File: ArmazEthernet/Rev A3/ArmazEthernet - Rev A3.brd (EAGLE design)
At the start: 72 x 80 mm, 125 parts, among them J1 22-05-7028-02, P1 RB1-125BAG1A, T1 H1102FNL, T2 H1102FNL, U1 TC1264-3.3, U2 TC1264-1.8, U3 KSZ8995MA, U4 AT24C02C-SSHM-B, X1 NE8FAV, X2 NE8FAV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

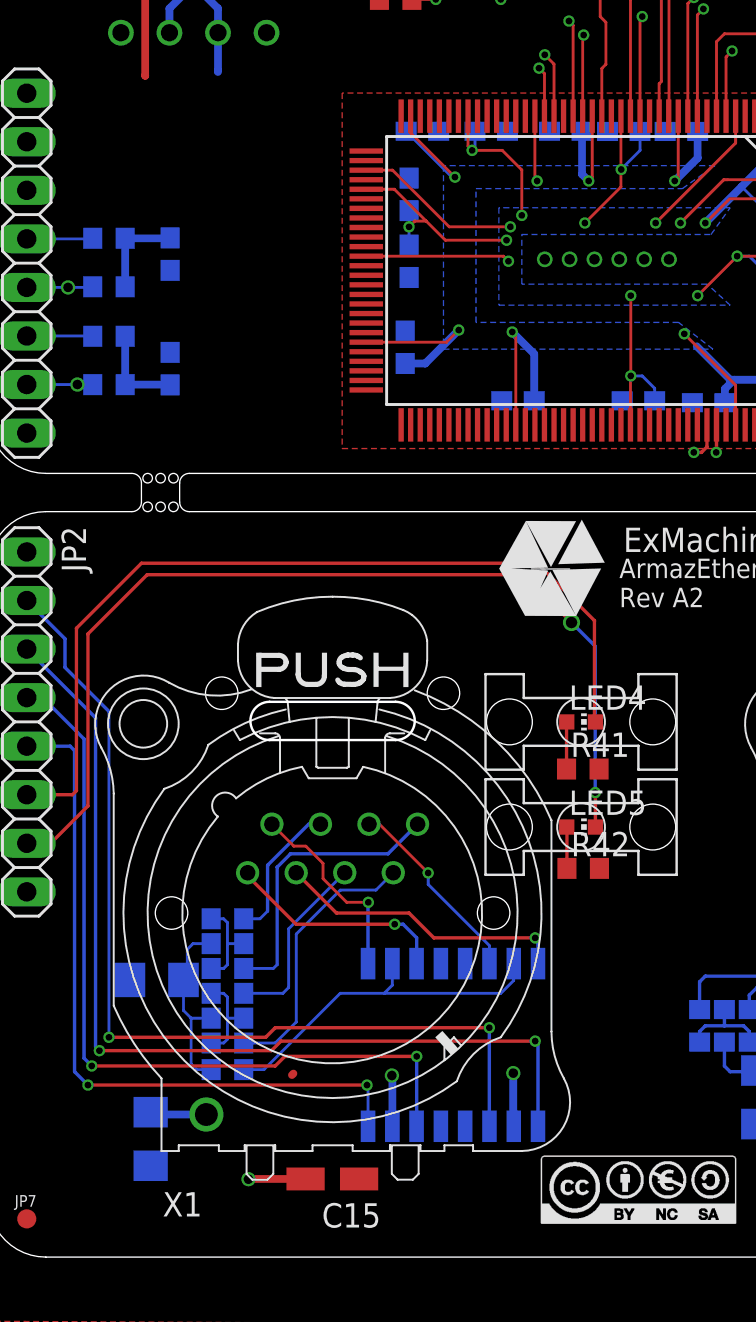
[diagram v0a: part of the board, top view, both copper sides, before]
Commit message: Move C46 and c12
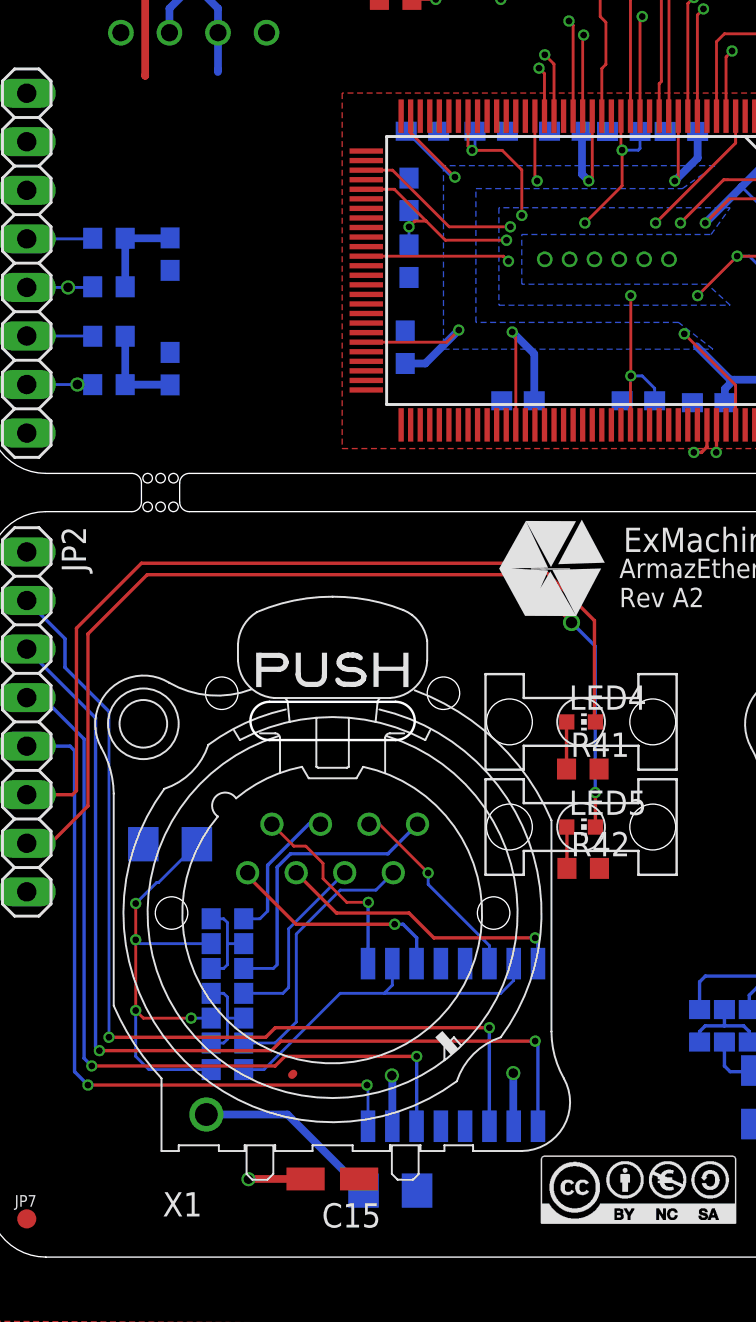
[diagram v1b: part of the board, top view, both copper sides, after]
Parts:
- moved C46 12.8 mm to (21.0, 3.48), turned to 180 degrees
- moved C12 7.13 mm to (9.50, 21.6)
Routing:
- net N$32: track 9.84 -> 24.9 mm, vias 0 -> 4
- net N$37: track 2.97 -> 9.87 mm
- net +1V8: track 128.3 -> 127.8 mm, vias 17 -> 18
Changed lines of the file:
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@@
 <layer number="19" name="Unrouted" color="6" fill="1" visible="yes" active="yes"/>
 <layer number="20" name="Dimension" color="15" fill="1" visible="yes" active="yes"/>
-<layer number="21" name="tPlace" color="7" fill="1" visible="yes" active="yes"/>
+<layer number="21" name="tPlace" color="7" fill="1" visible="no" active="yes"/>
 <layer number="22" name="bPlace" color="7" fill="1" visible="yes" active="yes"/>
-<layer number="23" name="tOrigins" color="15" fill="1" visible="yes" active="yes"/>
+<layer number="23" name="tOrigins" color="15" fill="1" visible="no" active="yes"/>
 <layer number="24" name="bOrigins" color="15" fill="1" visible="yes" active="yes"/>
-<layer number="25" name="tNames" color="7" fill="1" visible="yes" active="yes"/>
+<layer number="25" name="tNames" color="7" fill="1" visible="no" active="yes"/>
 <layer number="26" name="bNames" color="7" fill="1" visible="yes" active="yes"/>
-<layer number="27" name="tValues" color="7" fill="1" visible="yes" active="yes"/>
+<layer number="27" name="tValues" color="7" fill="1" visible="no" active="yes"/>
 <layer number="28" name="bValues" color="7" fill="1" visible="yes" active="yes"/>
 <layer number="29" name="tStop" color="7" fill="3" visible="no" active="yes"/>
@@
 <layer number="49" name="Reference" color="7" fill="1" visible="no" active="yes"/>
 <layer number="50" name="dxf" color="7" fill="1" visible="no" active="yes"/>
-<layer number="51" name="tDocu" color="7" fill="1" visible="yes" active="yes"/>
+<layer number="51" name="tDocu" color="7" fill="1" visible="no" active="yes"/>
 <layer number="52" name="bDocu" color="7" fill="1" visible="yes" active="yes"/>
 <layer number="91" name="Nets" color="2" fill="1" visible="no" active="no"/>
@@
 <layer number="95" name="Names" color="7" fill="1" visible="no" active="no"/>
 <layer number="96" name="Values" color="7" fill="1" visible="no" active="no"/>
-<layer number="2" name="Route2" color="38" fill="1" visible="yes" active="yes"/>
+<layer number="2" name="Route2" color="38" fill="1" visible="no" active="yes"/>
 <layer number="3" name="Route3" color="16" fill="1" visible="yes" active="yes"/>
 <layer number="14" name="Route14" color="1" fill="6" visible="no" active="no"/>
@@
 <attribute name="MPN" value="MC0063W0603175R" x="12.5" y="9.81" size="1.778" layer="28" rot="MR180" display="off"/>
 </element>
-<element name="C12" library="rcl" package="C1206" value="1000pF, 2kV" x="8.8" y="14.5" rot="MR0">
-<attribute name="OC_NEWARK" value="21T9879" x="8.8" y="14.5" size="1.778" layer="28" rot="MR0" display="off"/>
-<attribute name="MF" value="" x="8.8" y="14.5" size="1.778" layer="28" rot="MR0" display="off"/>
-<attribute name="MPN" value="MC1206B102K202CT" x="8.8" y="14.5" size="1.778" layer="28" rot="MR0" display="off"/>
+<element name="C12" library="rcl" package="C1206" value="1000pF, 2kV" x="9.5" y="21.6" rot="MR0">
+<attribute name="OC_NEWARK" value="21T9879" x="9.5" y="21.6" size="1.778" layer="28" rot="MR0" display="off"/>
+<attribute name="MF" value="" x="9.5" y="21.6" size="1.778" layer="28" rot="MR0" display="off"/>
+<attribute name="MPN" value="MC1206B102K202CT" x="9.5" y="21.6" size="1.778" layer="28" rot="MR0" display="off"/>
 </element>
 <element name="R7" library="rcl" package="R0603" value="51" x="38.5" y="12.1" rot="MR90">
@@
 <attribute name="MPN" value="1N4148W" x="50.27" y="69.8" size="1.778" layer="28" rot="MR90" display="off"/>
 </element>
-<element name="C46" library="rcl" package="C1206" value="1000pF, 2kV" x="8.48" y="6.18" rot="MR270">
-<attribute name="OC_NEWARK" value="21T9879" x="8.48" y="6.18" size="1.778" layer="28" rot="MR270" display="off"/>
-<attribute name="MF" value="" x="8.48" y="6.18" size="1.778" layer="28" rot="MR270" display="off"/>
-<attribute name="MPN" value="MC1206B102K202CT" x="8.48" y="6.18" size="1.778" layer="28" rot="MR270" display="off"/>
+<element name="C46" library="rcl" package="C1206" value="1000pF, 2kV" x="21.02" y="3.48" rot="MR180">
+<attribute name="OC_NEWARK" value="21T9879" x="21.02" y="3.48" size="1.778" layer="28" rot="MR180" display="off"/>
+<attribute name="MF" value="" x="21.02" y="3.48" size="1.778" layer="28" rot="MR180" display="off"/>
+<attribute name="MPN" value="MC1206B102K202CT" x="21.02" y="3.48" size="1.778" layer="28" rot="MR180" display="off"/>
 </element>
 <element name="C47" library="rcl" package="C1206" value="1000pF, 2kV" x="43.93" y="4.67" rot="MR0">
@@
 <contactref element="C12" pad="1"/>
 <contactref element="R6" pad="1"/>
-<wire x1="11.65" y1="16.4" x2="10.7" y2="16.4" width="0.15" layer="16"/>
-<wire x1="10.7" y1="16.4" x2="10.4" y2="16.1" width="0.15" layer="16"/>
-<wire x1="10.4" y1="16.1" x2="10.4" y2="14.7" width="0.15" layer="16"/>
-<wire x1="10.4" y1="14.7" x2="10.2" y2="14.5" width="0.15" layer="16"/>
-<wire x1="10.2" y1="14.5" x2="10.2" y2="12.9" width="0.15" layer="16"/>
-<wire x1="10.2" y1="12.9" x2="10.6" y2="12.5" width="0.15" layer="16"/>
+<wire x1="11.65" y1="9.81" x2="8.39" y2="9.81" width="0.15" layer="16"/>
+<wire x1="8.39" y1="9.81" x2="7.7" y2="10.5" width="0.15" layer="16"/>
+<wire x1="7.7" y1="10.5" x2="7.7" y2="12.9" width="0.15" layer="16"/>
+<wire x1="7.7" y1="12.9" x2="7.7" y2="16.6" width="0.15" layer="1"/>
+<wire x1="7.7" y1="16.6" x2="7.7" y2="18.5" width="0.15" layer="1"/>
+<wire x1="7.7" y1="18.5" x2="8.8" y2="19.6" width="0.15" layer="16"/>
+<wire x1="8.8" y1="19.6" x2="8.9" y2="19.6" width="0.15" layer="16"/>
+<wire x1="8.9" y1="19.6" x2="10.9" y2="21.6" width="0.15" layer="16"/>
+<wire x1="11.65" y1="16.4" x2="7.9" y2="16.4" width="0.15" layer="16"/>
+<wire x1="7.9" y1="16.4" x2="7.7" y2="16.6" width="0.15" layer="16"/>
+<wire x1="10.6" y1="12.5" x2="8.1" y2="12.5" width="0.15" layer="1"/>
+<wire x1="8.1" y1="12.5" x2="7.7" y2="12.9" width="0.15" layer="1"/>
+<via x="7.7" y="16.6" extent="1-16" drill="0.35"/>
+<via x="7.7" y="18.5" extent="1-16" drill="0.35"/>
+<via x="7.7" y="12.9" extent="1-16" drill="0.35"/>
+<via x="10.6" y="12.5" extent="1-16" drill="0.35"/>
 <wire x1="10.6" y1="12.5" x2="11.65" y2="12.5" width="0.15" layer="16"/>
-<wire x1="11.65" y1="9.81" x2="10.89" y2="9.81" width="0.15" layer="16"/>
-<wire x1="10.89" y1="9.81" x2="10.6" y2="10.1" width="0.15" layer="16"/>
-<wire x1="10.6" y1="10.1" x2="10.6" y2="12.5" width="0.15" layer="16"/>
 </signal>
 <signal name="N$10">
@@
 </polygon>
 <wire x1="39.085" y1="59.6922" x2="39.085" y2="58.6" width="0.15" layer="1"/>
-<wire x1="33.085" y1="59.6922" x2="33.085" y2="55.985" width="0.15" layer="1"/>
 <wire x1="19.7606" y1="55.865" x2="21.235" y2="55.865" width="0.15" layer="1"/>
 <wire x1="21.235" y1="55.865" x2="22.9" y2="54.2" width="0.15" layer="1"/>
@@
 <wire x1="26.935" y1="52.365" x2="27.2" y2="52.1" width="0.15" layer="1"/>
 <via x="27.2" y="52.1" extent="1-16" drill="0.35"/>
-<wire x1="33.085" y1="55.985" x2="31.2" y2="54.1" width="0.15" layer="1"/>
+<wire x1="33.147" y1="56.047" x2="31.2" y2="54.1" width="0.15" layer="1"/>
 <wire x1="41.9094" y1="56.365" x2="38.665" y2="56.365" width="0.15" layer="1"/>
 <wire x1="39.165" y1="52.365" x2="37.1" y2="50.3" width="0.15" layer="1"/>
@@
 <wire x1="22.3" y1="54.2" x2="22.9" y2="54.2" width="0.15" layer="1"/>
 <wire x1="22" y1="54.75" x2="22" y2="53.9" width="0.15" layer="16"/>
-<wire x1="34.085" y1="58.89" x2="34.085" y2="57.9" width="0.15" layer="16"/>
-<wire x1="34.085" y1="57.9" x2="33.085" y2="56.9" width="0.15" layer="16"/>
+<wire x1="34.085" y1="58.89" x2="34.085" y2="58" width="0.15" layer="16"/>
 <wire x1="42.2" y1="55.15" x2="40.25" y2="55.15" width="0.15" layer="16"/>
 <wire x1="40.25" y1="55.15" x2="39.4" y2="56" width="0.15" layer="16"/>
@@
 <wire x1="41.9094" y1="52.365" x2="39.165" y2="52.365" width="0.15" layer="1"/>
 <wire x1="42.2" y1="49.95" x2="42.2" y2="51.85" width="0.15" layer="16"/>
-<wire x1="33.085" y1="55.985" x2="33.085" y2="56.9" width="0" layer="19" extent="1-16"/>
+<wire x1="33.147" y1="56.047" x2="33.147" y2="57.912" width="0.15" layer="1"/>
+<via x="33.147" y="57.912" extent="1-16" drill="0.35"/>
+<wire x1="33.147" y1="57.912" x2="33.997" y2="57.912" width="0.15" layer="16"/>
+<wire x1="33.997" y1="57.912" x2="34.085" y2="58" width="0.15" layer="16"/>
+<wire x1="33.085" y1="59.6922" x2="33.085" y2="57.974" width="0.15" layer="1"/>
+<wire x1="33.085" y1="57.974" x2="33.147" y2="57.912" width="0.15" layer="1"/>
 </signal>
 <signal name="N$3">
@@
 <contactref element="X1" pad="G"/>
 <contactref element="C46" pad="1"/>
-<wire x1="11.396" y1="7.459" x2="8.601" y2="7.459" width="0.4064" layer="16"/>
-<wire x1="8.601" y1="7.459" x2="8.48" y2="7.58" width="0.4064" layer="16"/>
+<wire x1="11.396" y1="7.459" x2="15.641" y2="7.459" width="0.4064" layer="16"/>
+<wire x1="15.641" y1="7.459" x2="19.62" y2="3.48" width="0.4064" layer="16"/>
 </signal>
 <signal name="N$2">
@@
 <wire x1="46.7" y1="78.75" x2="48.4" y2="78.75" width="0.1778" layer="1"/>
 </signal>
-<signal name="N$24">
-<via x="33.1" y="56.9" extent="1-16" drill="0.35"/>
-</signal>
 </signals>

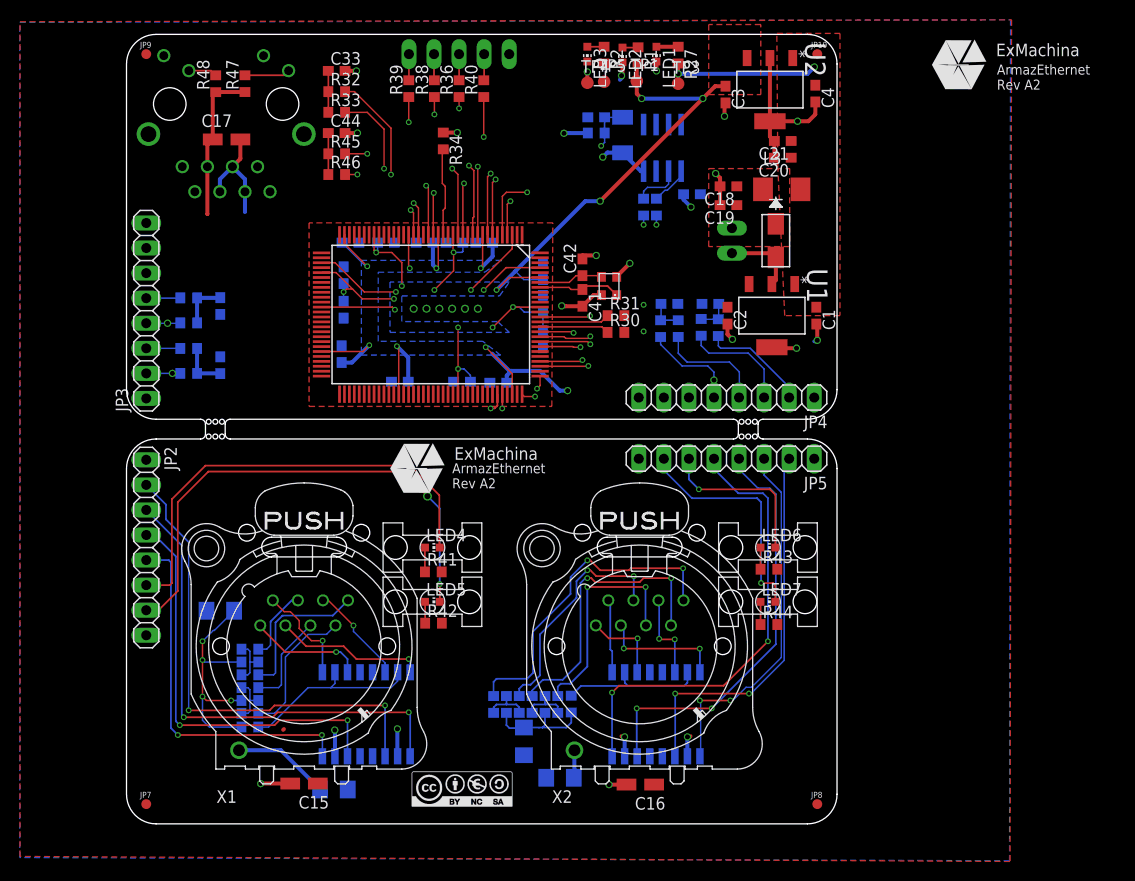
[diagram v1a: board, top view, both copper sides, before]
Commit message: Invert the GND plan and the power 3V3 plan and space the Ethernet signal to have a GND plan between two Ethernet signal
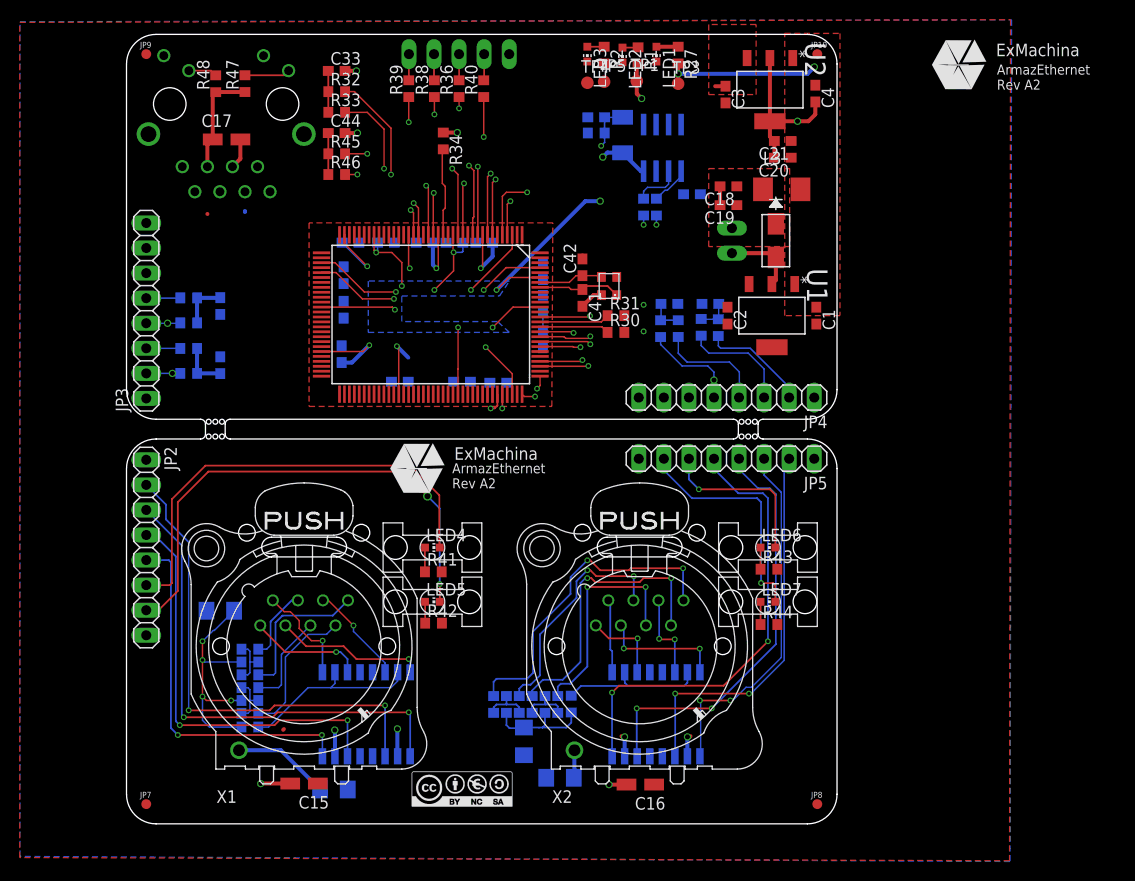
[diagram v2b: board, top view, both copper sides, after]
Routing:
- net +1V8: track 127.8 -> 93.7 mm, vias 18 -> 14
- net GND: track 69.0 -> 42.1 mm, vias 23 -> 6
- net +3V3: track 93.2 -> 71.2 mm, vias 15 -> 12
- removed copper zone on layer 1, net +3V3
- removed copper zone on layer 16, net GND

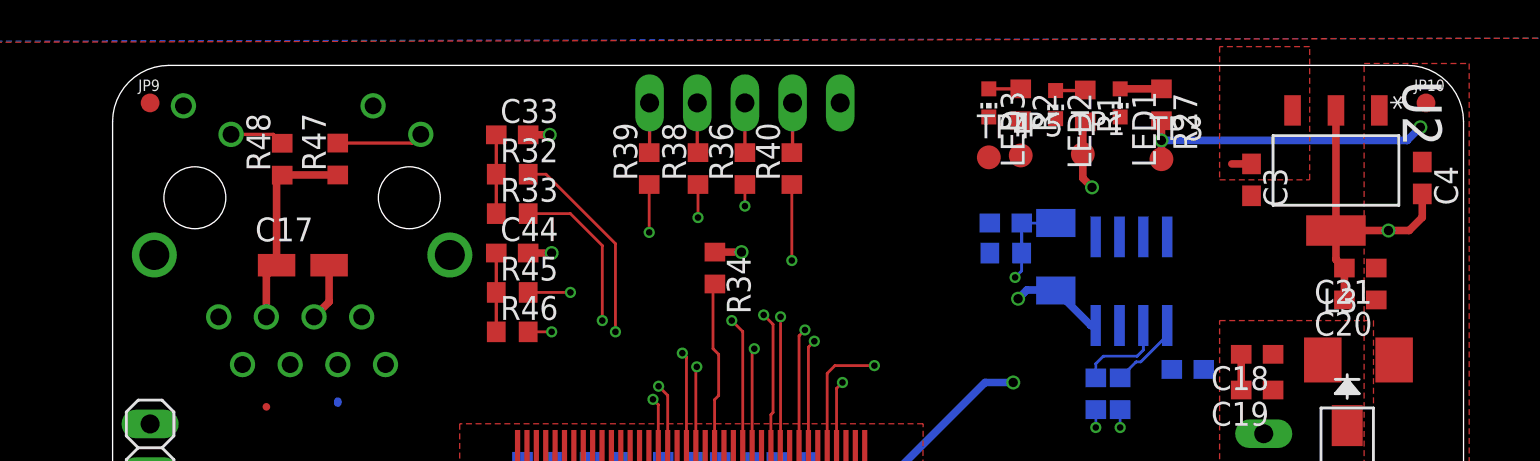
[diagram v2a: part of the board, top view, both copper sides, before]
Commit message: reroute all the panel with the power
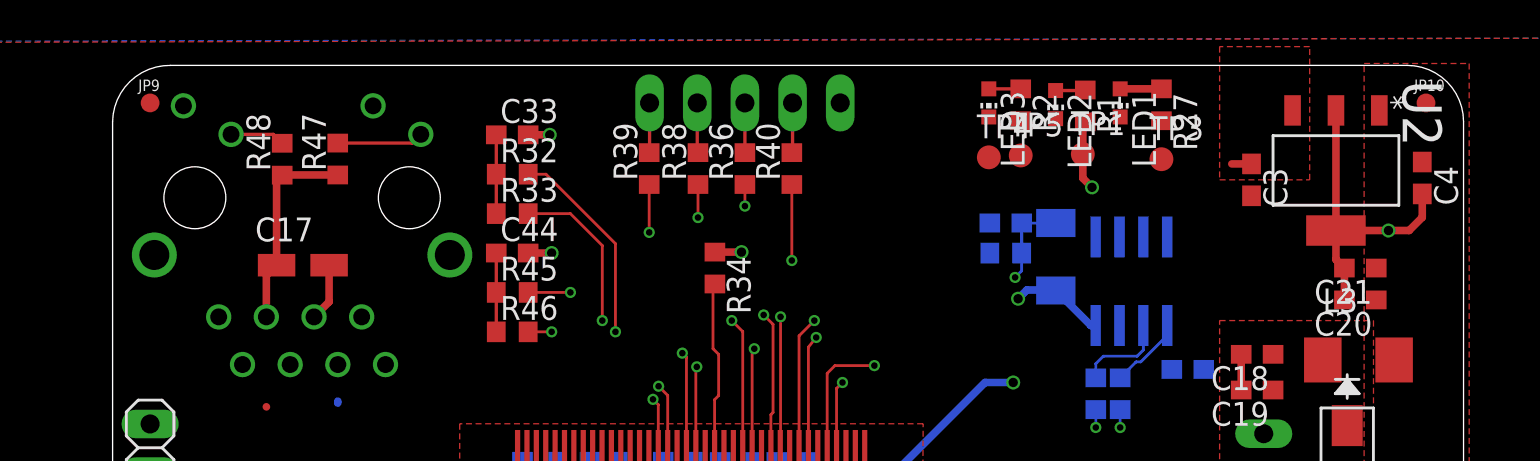
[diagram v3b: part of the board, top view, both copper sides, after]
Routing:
- net +5V: track 16.4 -> 0.26 mm, vias 2 -> 0
- net TX2_ISO_P: track 99.2 -> 99.9 mm
- net TX2_ISO_N: track 105.5 -> 106.2 mm
- net TX1_ISO_N: track 94.4 -> 93.7 mm
- added copper zone on layer 2, net GND
- added copper zone on layer 3, net GND
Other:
- outline, holes or cut-outs redrawn

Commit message: Finalize to reroute all the board
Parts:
- moved C43 11.1 mm to (46.2, 62.8), flipped to the top, turned to 0 degrees
- moved C45 8.36 mm to (55.9, 70.6), flipped to the top
- moved R49 8.36 mm to (55.9, 69.0), flipped to the top
- moved U4 5.20 mm to (49.2, 67.5), flipped to the top
- moved R35 4.03 mm to (49.8, 61.5), flipped to the top
- moved U$9 3.12 mm to (53.2, 68.8), flipped to the top
- moved R37 1.64 mm to (51.1, 61.5), flipped to the top
- moved LED3 0.50 mm to (46.2, 78.0)
- moved TP4 0.50 mm to (46.2, 75.1)
- moved C29 0.20 mm to (22.0, 47.6)
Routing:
- net GND: track 42.1 -> 63.4 mm, vias 6 -> 16
- net +5V: track 0.26 -> 18.6 mm, vias 0 -> 2
- net +3V3: track 71.2 -> 63.9 mm, vias 12 -> 22
- net +1V8: track 93.7 -> 100.5 mm
- net RST_N: track 28.1 -> 34.4 mm, vias 2 -> 3
- net SCL: track 56.2 -> 54.1 mm
- net SDA: track 54.2 -> 55.8 mm, vias 3 -> 4
- net N$6: track 1.70 -> 2.20 mm
- added copper zone on layer 1, net +3V3
